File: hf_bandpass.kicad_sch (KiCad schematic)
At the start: 20 parts

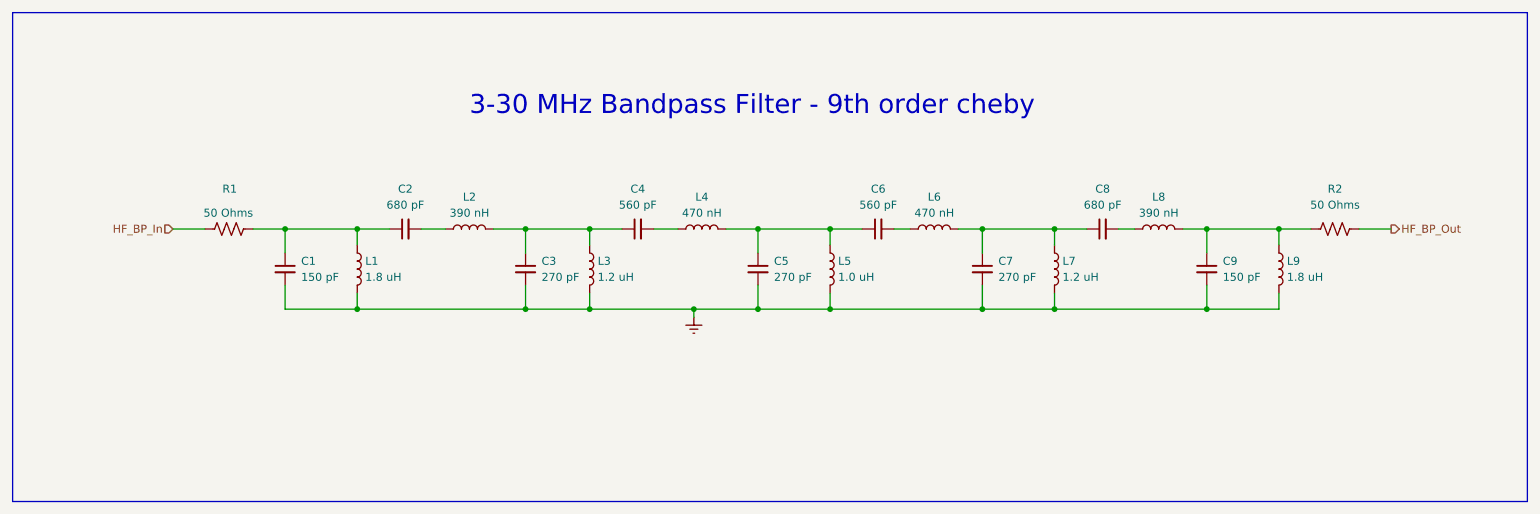
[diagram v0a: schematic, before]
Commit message: Redefined filters & Top Level Diagram
- Implement wider filters to accomodate 10% tolerance parts.
- Break design in to top-level heirarchical blocks.
- Start wiring some of the blocks together.
- Add L-Band segment, but is currently just a copy of the UHF filter.
- Add the start of a TX path.
- Add placeholders for power and band/tune control.
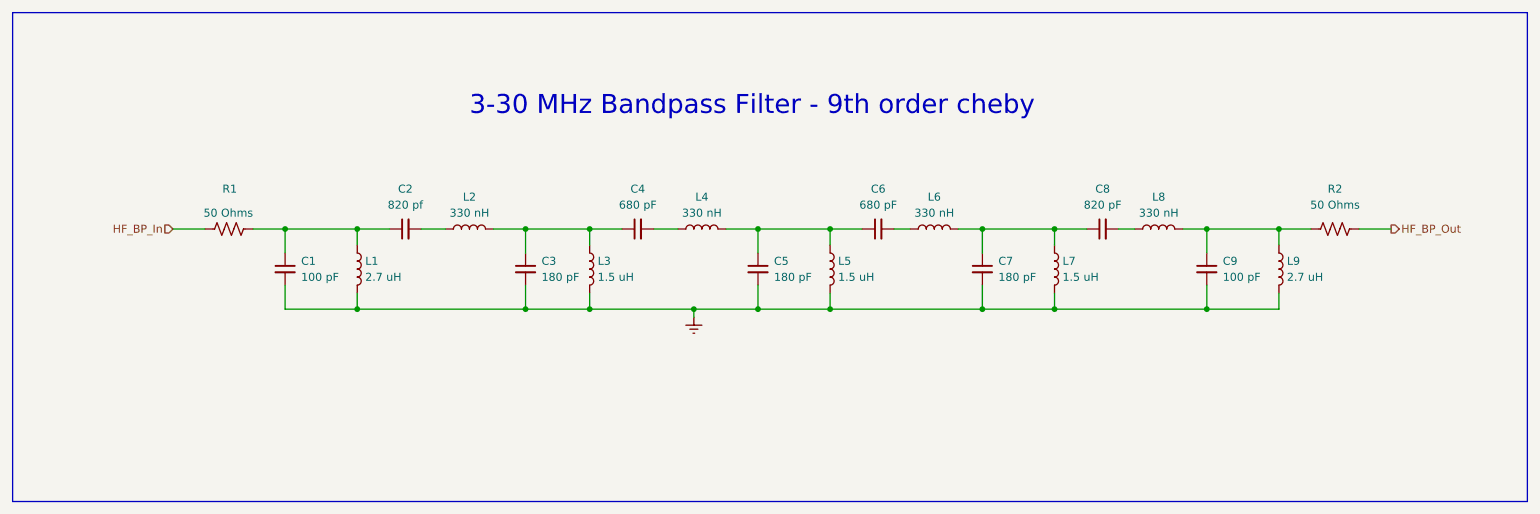
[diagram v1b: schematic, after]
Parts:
- C1, C9: value 150 pF -> 100 pF; footprint Capacitor_SMD:C_0805_2012Metric_Pad1.18x1.45mm_HandSolder -> Capacitor_SMD:C_1206_3216Metric
- C2: value 680 pF -> 820 pf; footprint Capacitor_SMD:C_0805_2012Metric_Pad1.18x1.45mm_HandSolder -> Capacitor_SMD:C_1206_3216Metric
- C3, C5, C7: value 270 pF -> 180 pF; footprint Capacitor_SMD:C_0805_2012Metric_Pad1.18x1.45mm_HandSolder -> Capacitor_SMD:C_1206_3216Metric
- C4, C6: value 560 pF -> 680 pF; footprint Capacitor_SMD:C_0805_2012Metric_Pad1.18x1.45mm_HandSolder -> Capacitor_SMD:C_1206_3216Metric
- C8: value 680 pF -> 820 pF; footprint Capacitor_SMD:C_0805_2012Metric_Pad1.18x1.45mm_HandSolder -> Capacitor_SMD:C_1206_3216Metric
- L1, L9: value 1.8 uH -> 2.7 uH; footprint Inductor_SMD:L_0805_2012Metric_Pad1.05x1.20mm_HandSolder -> Inductor_SMD:L_1206_3216Metric
- L2, L8: value 390 nH -> 330 nH; footprint Inductor_SMD:L_0805_2012Metric_Pad1.05x1.20mm_HandSolder -> Inductor_SMD:L_1206_3216Metric
- L3, L7: value 1.2 uH -> 1.5 uH; footprint Inductor_SMD:L_0805_2012Metric_Pad1.05x1.20mm_HandSolder -> Inductor_SMD:L_1206_3216Metric
- L4, L6: value 470 nH -> 330 nH; footprint Inductor_SMD:L_0805_2012Metric_Pad1.05x1.20mm_HandSolder -> Inductor_SMD:L_1206_3216Metric
- L5: value 1.0 uH -> 1.5 uH; footprint Inductor_SMD:L_0805_2012Metric_Pad1.05x1.20mm_HandSolder -> Inductor_SMD:L_1206_3216Metric

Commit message: More filter work. Add project title to drawings.
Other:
- company: (none) -> Steves Custom Computers
- title: (none) -> PLUTO RF Card Front-End
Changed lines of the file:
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@@
 (kicad_sch (version 20230121) (generator eeschema)
   (paper "A4")
+  (title_block
+    (title "PLUTO RF Card Front-End")
+    (rev " 001")
+    (company "Steves Custom Computers")
+  )
   (junction (at 119.38 106.68) (diameter 0) (color 0 0 0 0)
   )

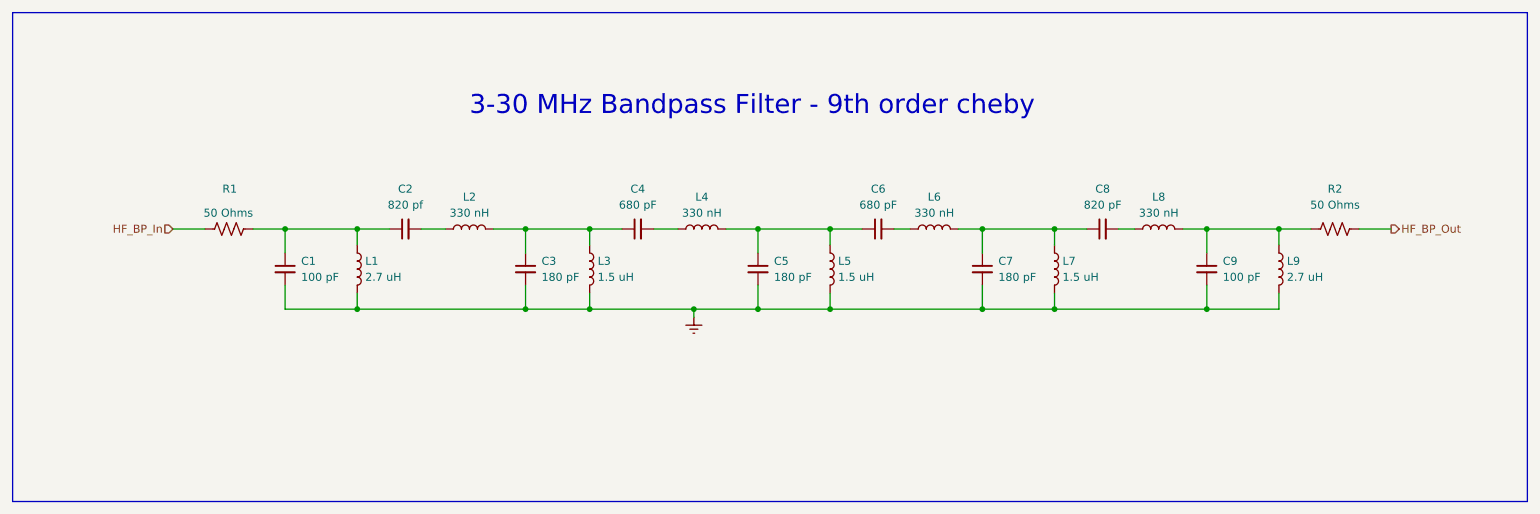
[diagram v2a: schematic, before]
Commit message: Major restructure. Add power/control busses.
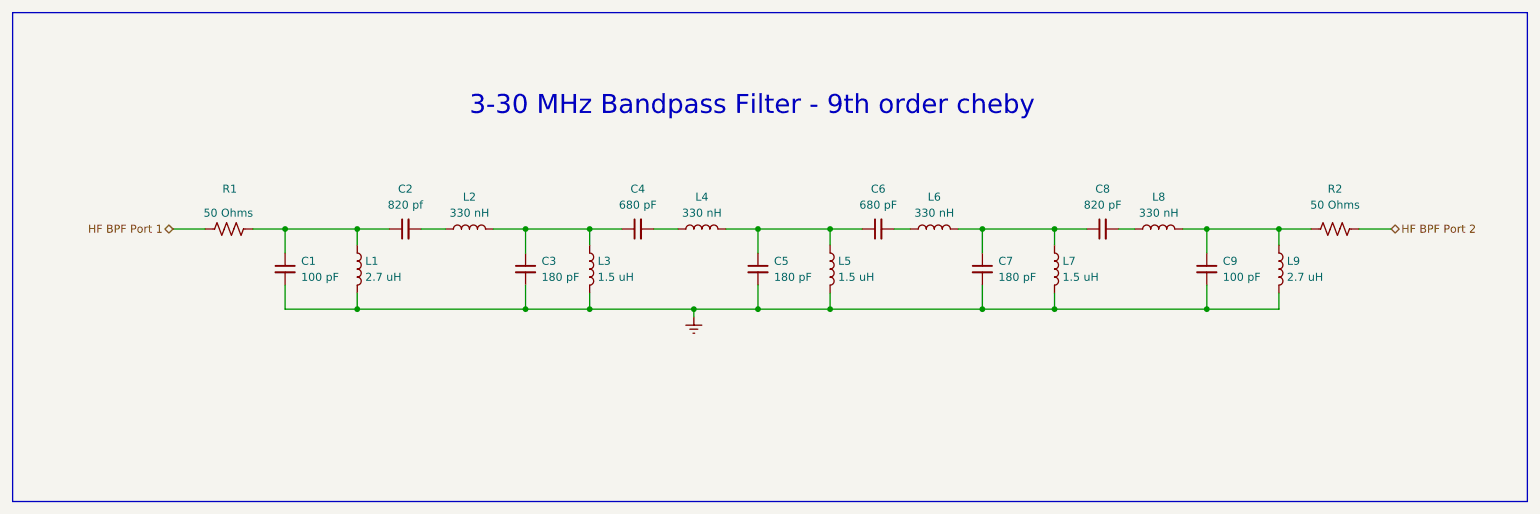
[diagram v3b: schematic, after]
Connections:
- net HF_BP_In renamed HF BPF Port 1
- net HF_BP_Out renamed HF BPF Port 2
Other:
- title: PLUTO RF Card Front-End -> PLUTO RF Front-End Card
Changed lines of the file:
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@@
   (paper "A4")
   (title_block
-    (title "PLUTO RF Card Front-End")
+    (title "PLUTO RF Front-End Card")
     (rev " 001")
     (company "Steves Custom Computers")
@@
     (effects (font (size 3 3)) (justify left bottom))
   )
-  (hierarchical_label "HF_BP_Out" (shape output) (at 246.38 93.98 0) (fields_autoplaced)
+  (hierarchical_label "HF BPF Port 2" (shape bidirectional) (at 246.38 93.98 0) (fields_autoplaced)
     (effects (font (size 1.27 1.27)) (justify left))
   )
-  (hierarchical_label "HF_BP_In" (shape input) (at 53.34 93.98 180) (fields_autoplaced)
+  (hierarchical_label "HF BPF Port 1" (shape bidirectional) (at 53.34 93.98 180) (fields_autoplaced)
     (effects (font (size 1.27 1.27)) (justify right))
   )
